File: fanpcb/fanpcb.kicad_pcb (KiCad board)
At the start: 2 copper layers, 30 x 50 mm, 16 parts, among them M1 Fan_4pin, M2 Fan_4pin, M3 Fan_4pin, T1 TACHO, T12V1 TestPoint, T2 TACHO, T3 TACHO

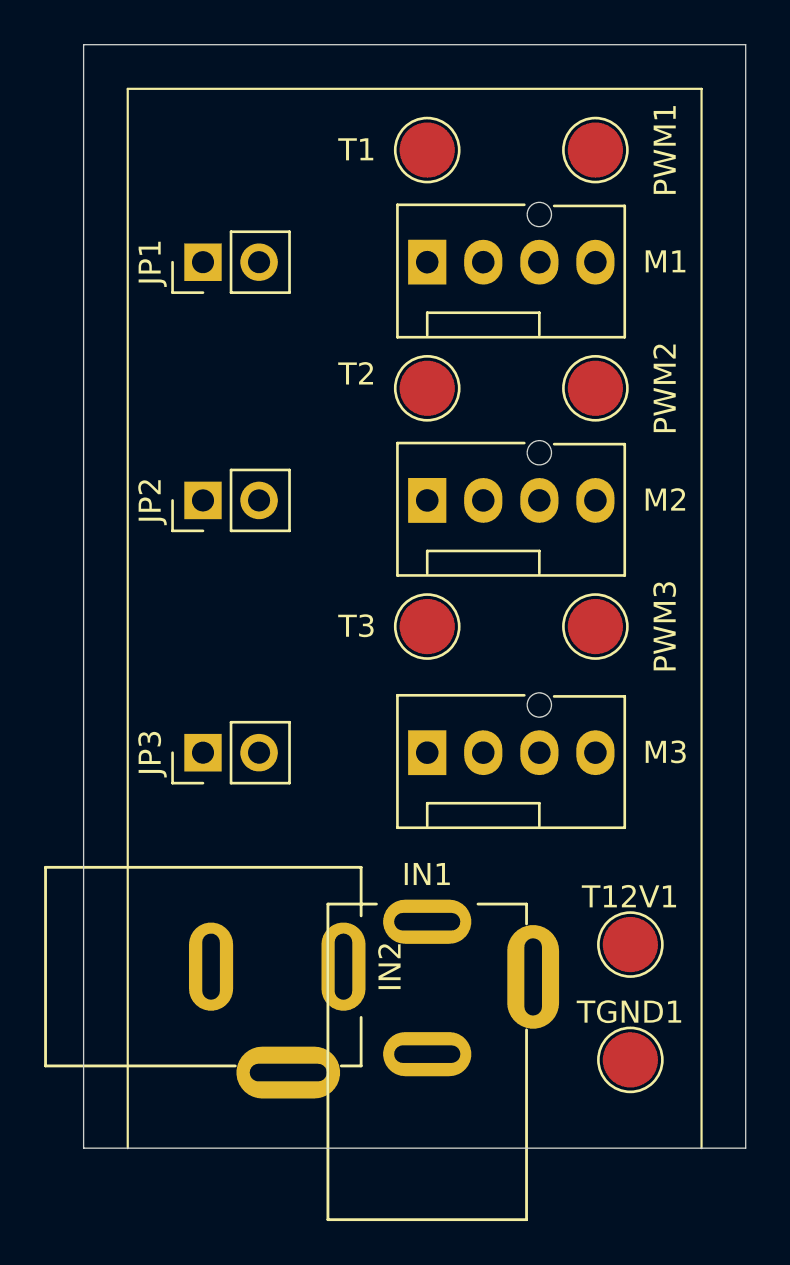
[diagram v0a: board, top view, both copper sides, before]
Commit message: fanpcb geroutet und gnd
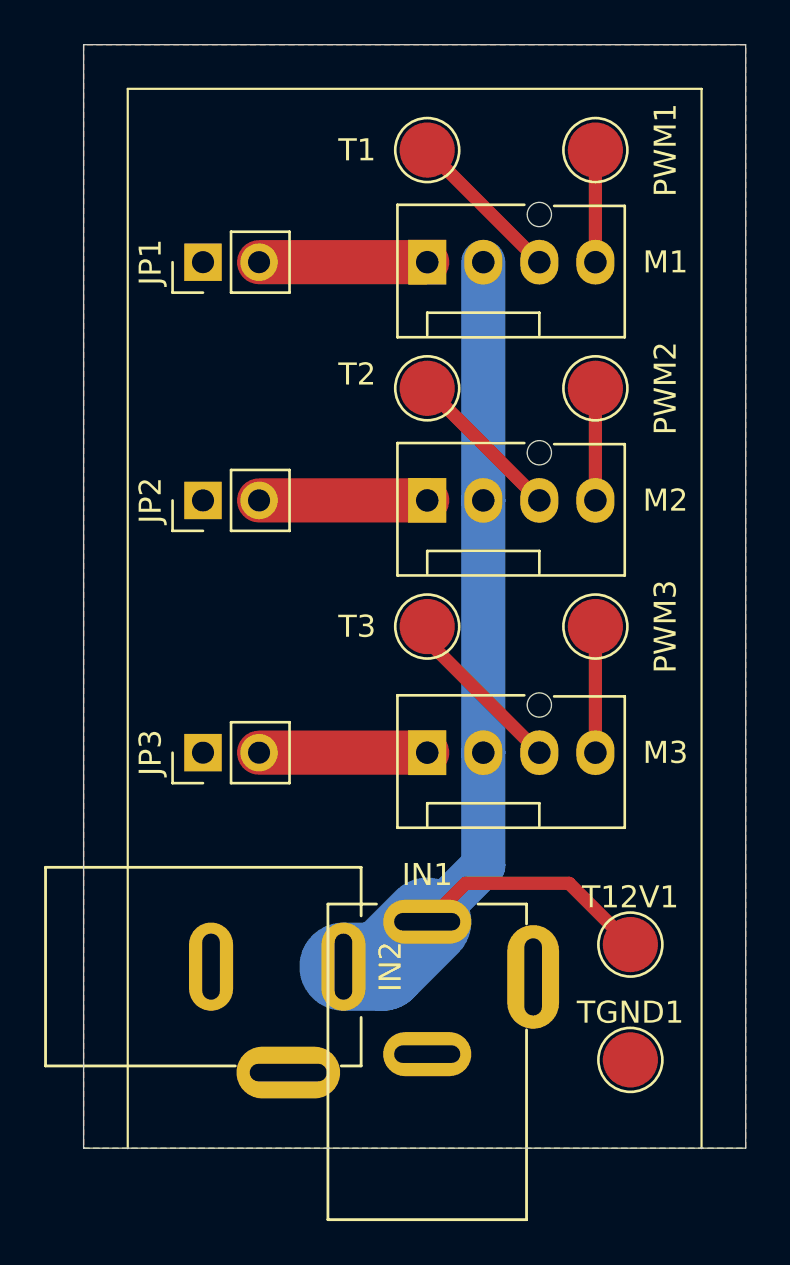
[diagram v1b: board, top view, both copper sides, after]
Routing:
- net +12V: track 0.00 -> 46.7 mm
- net Net-(M3-Tacho): track 0.00 -> 7.82 mm
- net Net-(JP3-B): track 0.00 -> 7.62 mm
- net Net-(JP2-B): track 0.00 -> 7.62 mm
- net Net-(JP1-B): track 0.00 -> 7.62 mm
- net Net-(M2-Tacho): track 0.00 -> 7.18 mm
- net Net-(M1-Tacho): track 0.00 -> 7.18 mm
- net Net-(M3-PWM): track 0.00 -> 5.72 mm
- net Net-(M2-PWM): track 0.00 -> 5.08 mm
- net Net-(M1-PWM): track 0.00 -> 5.08 mm
- added copper zone on B.Cu, net GND
- added copper zone on F.Cu, net GND
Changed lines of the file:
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@@
 		(layer "Edge.Cuts")
+	)
+	(segment
+		(start 123.19 132.08)
+		(end 123.19 126.365)
+		(width 0.6)
+		(layer "F.Cu")
+		(net "Net-(M3-PWM)")
+	)
+	(segment
+		(start 123.19 120.65)
+		(end 123.19 115.57)
+		(width 0.6)
+		(layer "F.Cu")
+		(net "Net-(M2-PWM)")
+	)
+	(segment
+		(start 122 138)
+		(end 117.31 138)
+		(width 0.6)
+		(layer "F.Cu")
+		(net "+12V")
+	)
+	(segment
+		(start 124.775 140.775)
+		(end 122 138)
+		(width 0.6)
+		(layer "F.Cu")
+		(net "+12V")
+	)
+	(segment
+		(start 117.31 138)
+		(end 115.57 139.74)
+		(width 0.6)
+		(layer "F.Cu")
+		(net "+12V")
+	)
+	(segment
+		(start 118.11 109.855)
+		(end 118.11 120.65)
+		(width 2)
+		(layer "B.Cu")
+		(net "+12V")
+	)
+	(segment
+		(start 113.535 141.775)
+		(end 115.57 139.74)
+		(width 4)
+		(layer "B.Cu")
+		(net "+12V")
+	)
+	(segment
+		(start 111.775 141.775)
+		(end 113.535 141.775)
+		(width 4)
+		(layer "B.Cu")
+		(net "+12V")
+	)
+	(segment
+		(start 118.11 137.2)
+		(end 115.57 139.74)
+		(width 2)
+		(layer "B.Cu")
+		(net "+12V")
+	)
+	(segment
+		(start 118.11 132.08)
+		(end 118.11 120.65)
+		(width 2)
+		(layer "B.Cu")
+		(net "+12V")
+	)
+	(segment
+		(start 118.11 132.08)
+		(end 118.11 137.2)
+		(width 2)
+		(layer "B.Cu")
+		(net "+12V")
+	)
+	(segment
+		(start 107.95 132.08)
+		(end 115.57 132.08)
+		(width 2)
+		(layer "F.Cu")
+		(net "Net-(JP3-B)")
+	)
+	(segment
+		(start 115.57 127)
+		(end 115.57 126.365)
+		(width 0.6)
+		(layer "F.Cu")
+		(net "Net-(M3-Tacho)")
+	)
+	(segment
+		(start 120.65 132.08)
+		(end 115.57 127)
+		(width 0.6)
+		(layer "F.Cu")
+		(net "Net-(M3-Tacho)")
+	)
+	(segment
+		(start 107.95 120.65)
+		(end 115.57 120.65)
+		(width 2)
+		(layer "F.Cu")
+		(net "Net-(JP2-B)")
+	)
+	(segment
+		(start 120.65 120.65)
+		(end 115.57 115.57)
+		(width 0.6)
+		(layer "F.Cu")
+		(net "Net-(M2-Tacho)")
+	)
+	(segment
+		(start 123.19 109.855)
+		(end 123.19 104.775)
+		(width 0.6)
+		(layer "F.Cu")
+		(net "Net-(M1-PWM)")
+	)
+	(segment
+		(start 120.65 109.855)
+		(end 115.57 104.775)
+		(width 0.6)
+		(layer "F.Cu")
+		(net "Net-(M1-Tacho)")
+	)
+	(segment
+		(start 107.95 109.855)
+		(end 115.57 109.855)
+		(width 2)
+		(layer "F.Cu")
+		(net "Net-(JP1-B)")
+	)
+	(zone
+		(net "GND")
+		(layers "F.Cu" "B.Cu")
+		(name "GND")
+		(hatch edge 0.5)
+		(connect_pads
+			(clearance 0.5)
+		)
+		(min_thickness 0.25)
+		(fill yes
+			(thermal_gap 0.5)
+			(thermal_bridge_width 0.5)
+			(island_removal_mode 0)
+		)
+		(polygon
+			(pts
+				(xy 100 100) (xy 100 150) (xy 130 150) (xy 130 100)
+			)
+		)
 	)
 	(embedded_fonts no)
